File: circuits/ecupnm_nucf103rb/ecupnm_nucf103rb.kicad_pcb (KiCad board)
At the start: 2 copper layers, 76 x 66 mm, 41 parts, among them J1 Conn_01x03_Pin, J2 USB_B_Mini, Q1 2N3904, Q2 IRF540N, Q3 IRF540N, U1 NUCLEO-64, U2 H11L1, U3 AMS1117-5.0, U4 4N35, U5 4N35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

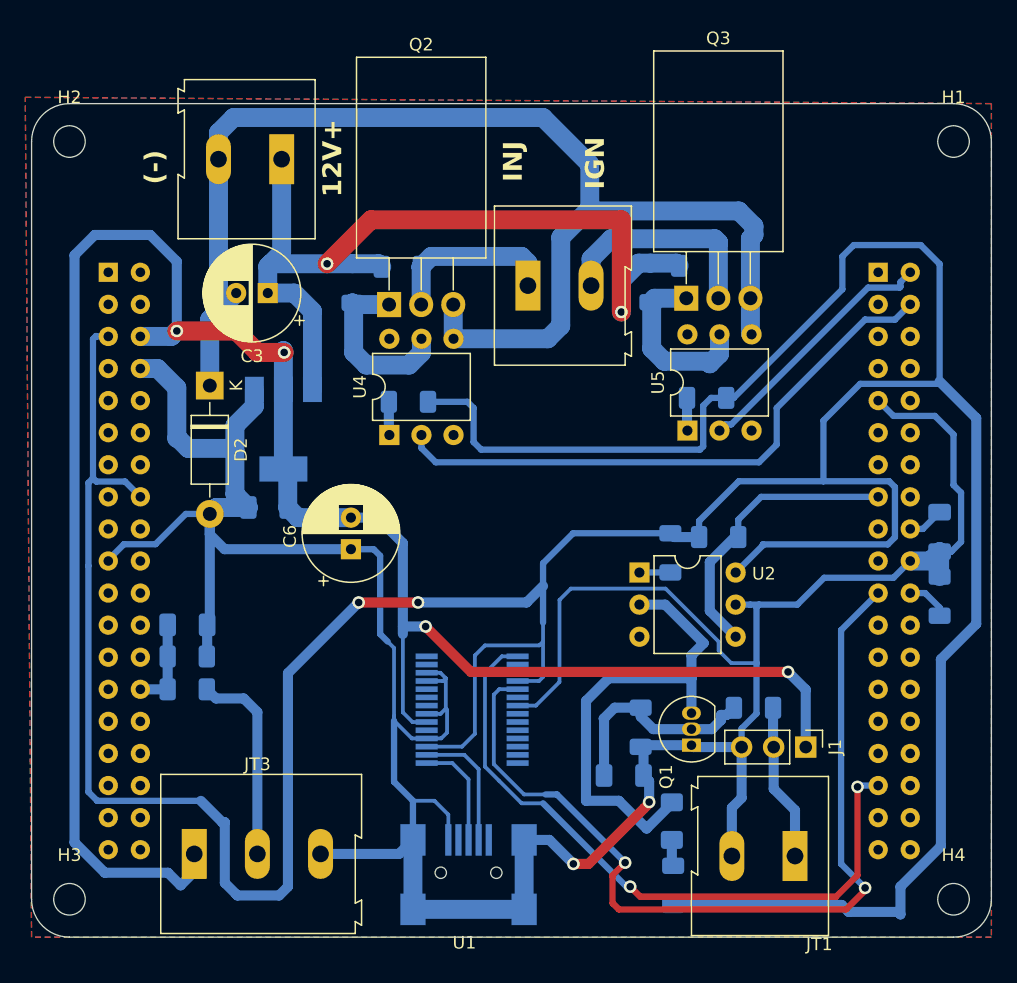
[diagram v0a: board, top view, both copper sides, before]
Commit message: Ganti Ukuran Vias
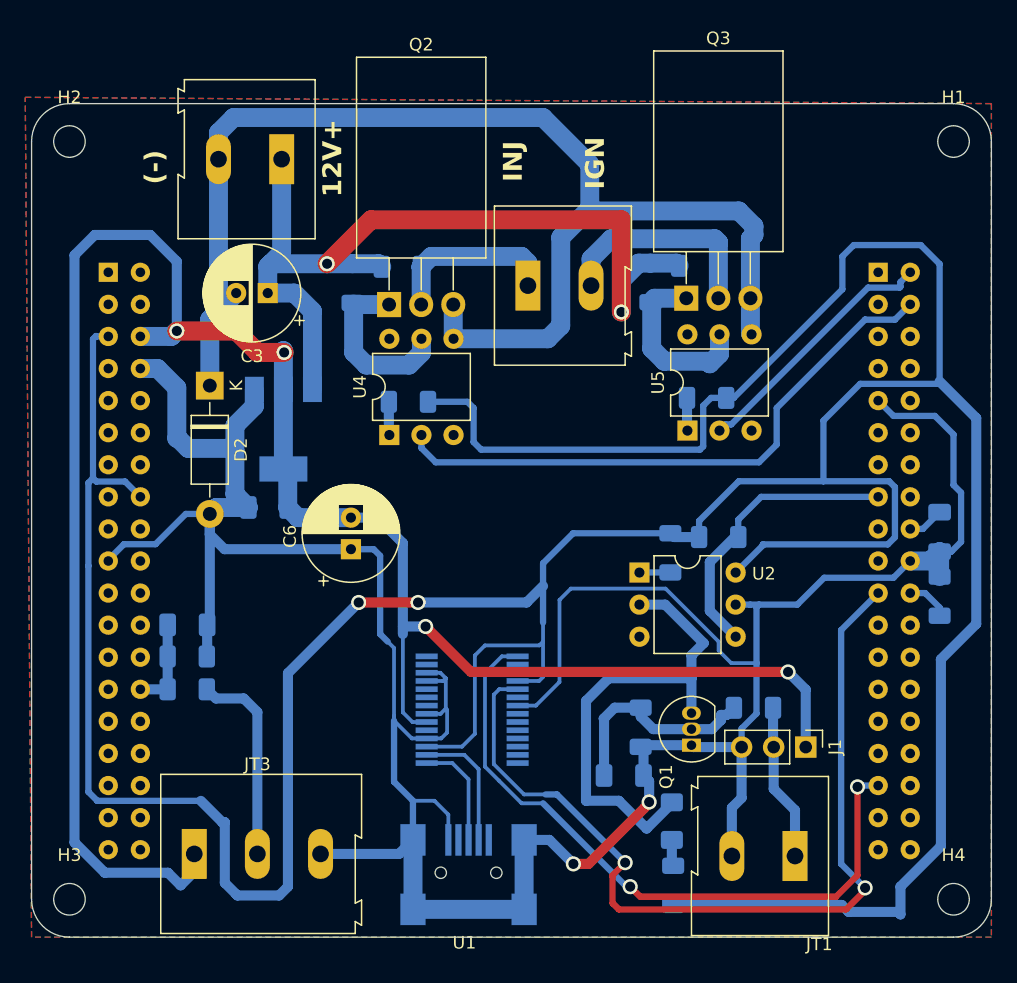
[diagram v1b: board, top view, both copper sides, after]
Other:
- board text added: "ECU BBG by Deny Nur"

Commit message: PCB Nucleo Notes
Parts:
- removed C6: 100uF, Capacitor_THT:CP_Radial_D7.5mm_P2.50mm
